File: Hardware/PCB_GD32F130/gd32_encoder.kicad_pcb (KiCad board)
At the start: 2 copper layers, 32 x 20 mm, 25 parts, among them J1 Conn_01x03_Pin, J2 Conn_01x03_Pin, J3 Conn_01x04_Pin, Q1 2N7002K, U1 XC6206PxxxMR, U2 MT6701CT, U3 GD32F130F4P6TR

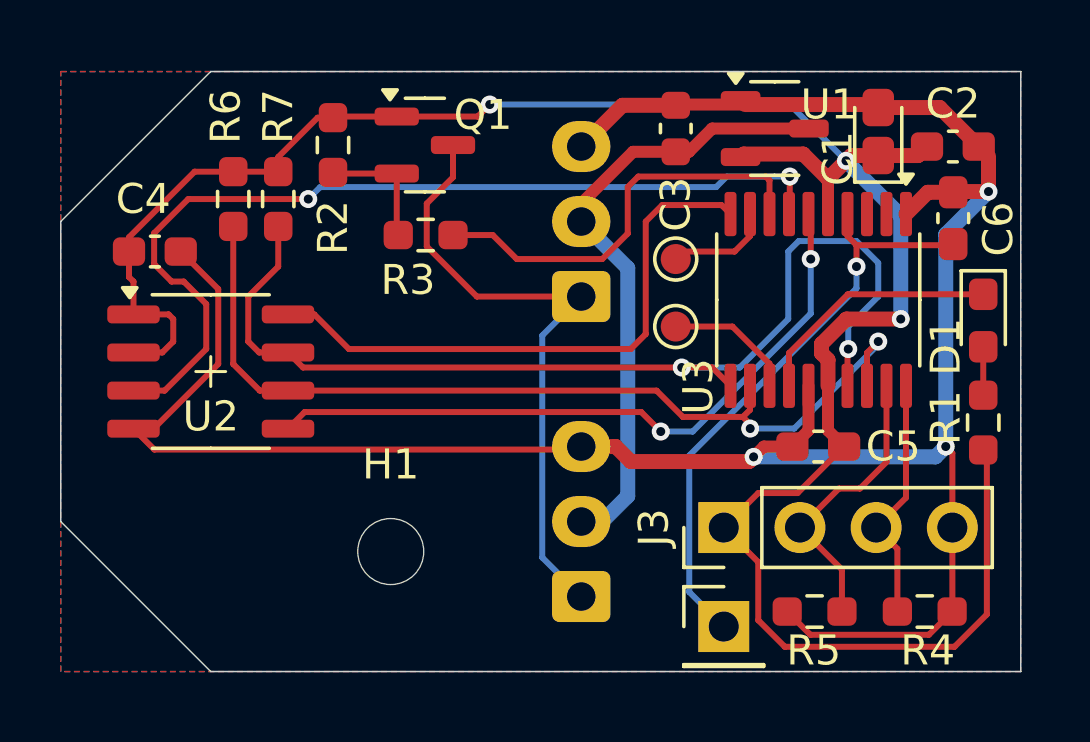
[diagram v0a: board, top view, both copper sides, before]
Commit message: Added PCB for CH32V003, which is a bit cheaper. New revision of GD32F130 PCB.
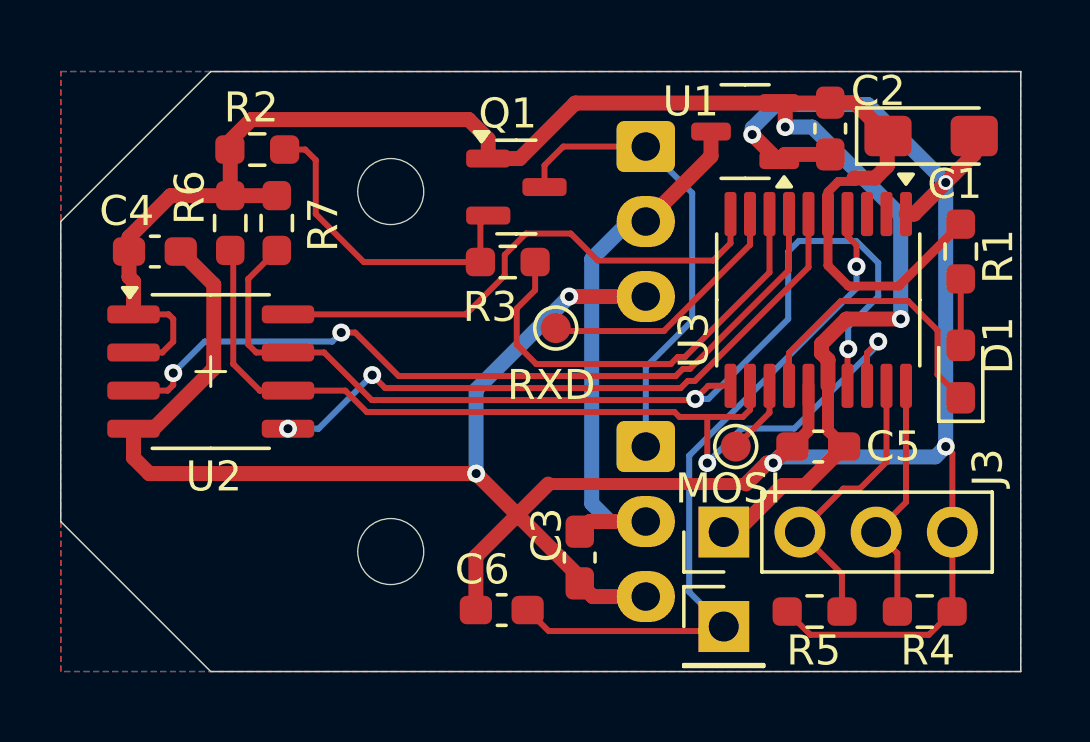
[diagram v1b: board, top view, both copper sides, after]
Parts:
- removed TP2: RXD, TestPoint:TestPoint_Pad_D1.0mm
- removed TP3: MOSI, TestPoint:TestPoint_Pad_D1.0mm
- added H2: MountingHole, MountingHole:MountingHole_2.2mm_M2_DIN965, F.Cu at (111.0, 104.0)
- added MOSI: MOSI, TestPoint:TestPoint_Pad_D1.0mm, F.Cu at (122.5, 112.5)
- added RXD: RXD, TestPoint:TestPoint_Pad_D1.0mm, F.Cu at (116.5, 108.5)
- C1: footprint Capacitor_Tantalum_SMD:CP_EIA-1608-10_AVX-L_Pad1.25x1.05mm_HandSolder -> Capacitor_Tantalum_SMD:CP_EIA-3216-18_Kemet-A_Pad1.58x1.35mm_HandSolder
- C3: footprint Capacitor_SMD:C_0603_1608Metric -> Capacitor_SMD:C_0603_1608Metric_Pad1.08x0.95mm_HandSolder
- moved C6 19.9 mm to (114.7, 118.0), turned to 180 degrees
- moved C3 14.7 mm to (117.3, 116.2), turned to -90 degrees
- moved R1 5.75 mm to (130.0, 106.0), turned to -90 degrees
- moved J1 5.44 mm to (119.5, 102.5), turned to -90 degrees
- moved J2 5.44 mm to (119.5, 112.5), turned to -90 degrees
- moved C2 4.13 mm to (125.7, 101.9), turned to -90 degrees
- moved Q1 3.36 mm to (115.2, 103.8)
- moved R3 2.88 mm to (114.9, 106.3)
- moved R2 2.53 mm to (106.5, 102.6), turned to 0 degrees
- moved D1 1.86 mm to (130.0, 110.0), turned to 90 degrees
- moved C1 1.77 mm to (129.0, 102.2), turned to 0 degrees
- moved U1 0.99 mm to (122.8, 102.0), turned to 180 degrees
- moved R6 0.81 mm to (105.7, 105.0)
- moved R7 0.80 mm to (107.2, 105.0)
- moved J3 0.15 mm to (122.1, 115.3)
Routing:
- net GND: track 78.2 -> 94.0 mm, vias 3 -> 6
- net +3.3V: track 76.4 -> 69.5 mm, vias 3 -> 2
- net Net-(Q1-S): track 4.09 -> 10.8 mm
- net Net-(U3-PA3/RX0): track 3.17 -> 8.59 mm
- net /Data: track 20.7 -> 15.6 mm
- net /Push: track 31.0 -> 26.8 mm
- net Net-(U3-NRST): track 19.8 -> 23.3 mm
- net /MISO/SDA: track 31.1 -> 33.1 mm
- net /MOSI: track 4.38 -> 2.49 mm
- net /SS: track 19.5 -> 17.9 mm
- net VCC: track 19.6 -> 18.2 mm
- net Net-(D1-K): track 8.38 -> 9.74 mm
- net /Out: track 22.8 -> 21.7 mm
- net /Com: track 14.1 -> 14.9 mm
- net Net-(D1-A): track 1.61 -> 2.21 mm
